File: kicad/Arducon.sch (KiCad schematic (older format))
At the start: 67 parts, among them J101 To Radio, J102 DB9 Female, J103 To Antenna, J104 Conn_01x08, J105 Conn_01x08, J106 Logic Level, J107 External Power Source, J108 Controlled Power, J109 Conn_01x01, J110 Conn_01x01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

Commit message: BOM Updates
Updated BOM
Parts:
- SJ110: renamed from SJ101; Link (none) -> np; Part No. (none) -> np
- SJ111: renamed from SJ102; Link (none) -> np; Part No. (none) -> np
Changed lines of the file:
@@
 Sheet 1 2
 Title "Arducon"
-Date "2021-02-24"
+Date "2021-03-03"
 Rev "P2.0"
 Comp ""
@@
 EXTERNAL_PWR_SOURCE
 $Comp
-L Jumper:SolderJumper_3_Bridged12 SJ102
+L Jumper:SolderJumper_3_Bridged12 SJ111
 U 1 1 60436DAC
 P 2150 6800
-F 0 "SJ102" V 2150 6867 50  0000 L CNN
+F 0 "SJ111" V 2150 6867 50  0000 L CNN
 F 1 "SolderJumper_3_Bridged12" V 2195 6868 50  0001 L CNN
 F 2 "Wire_Connections_Bridges:Solder-Jumperx3-NC_1-2_SMD-Pad_Small" H 2150 6800 50  0001 C CNN
-F 3 "~" H 2150 6800 50  0001 C CNN
+F 3 "" H 2150 6800 50  0001 C CNN
+F 4 "np" H 2150 6800 50  0001 C CNN "Part No."
+F 5 "np" H 2150 6800 50  0001 C CNN "Link"
 	1    2150 6800
 	0    -1   1    0
@@
 	3700 4750 3700 6150
 $Comp
-L Jumper:SolderJumper_3_Bridged12 SJ101
+L Jumper:SolderJumper_3_Bridged12 SJ110
 U 1 1 6050CA09
 P 2300 5550
-F 0 "SJ101" H 2300 5663 50  0000 C CNN
+F 0 "SJ110" H 2300 5663 50  0000 C CNN
 F 1 "SolderJumper_3_Bridged12" V 2345 5618 50  0001 L CNN
 F 2 "Wire_Connections_Bridges:Solder-Jumperx3-NC_1-2_SMD-Pad_Small" H 2300 5550 50  0001 C CNN
-F 3 "~" H 2300 5550 50  0001 C CNN
+F 3 "" H 2300 5550 50  0001 C CNN
+F 4 "np" H 2300 5550 50  0001 C CNN "Part No."
+F 5 "np" H 2300 5550 50  0001 C CNN "Link"
 	1    2300 5550
 	-1   0    0    1

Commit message: PCB Updates
PCB, Schematic, and BOM Updates
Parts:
- removed SJ109: SolderJumper_2_Open, Wire_Connections_Bridges:Solder-Jumper-NO-SMD-Pad_Small, symbol Jumper:SolderJumper_2_Open
- added SW102: 5V/12V, Buttons_Switches_SMD:SW_SPDT_PCM12, symbol Switch:SW_SPDT
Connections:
- net Controlled_Power: no longer J102.2
- net EXT_BATTERY: now also SW102.3 (C); no longer J102.7
- net Vproc: now also SW102.1 (A); no longer J102.4
- net DTR: now reaches MOD101.30 (DTR)
- net DTR: now also J102.2
- net CW_KEY: now reaches J106.3 (Pin_3), SJ110.2 (C)
- net CW_KEY: now also J102.4
- net ~RTC_INT~ renamed PD3
- new net RADIO_V+: J102.7, SW102.2 (B)
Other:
- moved on the sheet: C103, Q101, R101, R102, R104, RV101, SJ102

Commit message: Gerbers
Small updates to silkscreen layer
Small updates to schematic
Generated Gerber files for JLCPCB
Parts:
- removed SJ111: SolderJumper_3_Bridged12, Wire_Connections_Bridges:Solder-Jumperx3-NC_1-2_SMD-Pad_Small, symbol Jumper:SolderJumper_3_Bridged12
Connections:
- net RADIO_V+ is gone; now on net Power_In: J102.7, SW102.2 (B)
- net Power_In: now reaches R107.2
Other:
- moved on the sheet: C103, C109, R101, R102, R107, R108, RV101, SJ102, SW102

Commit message: TVS Diode Substitution
Substituted an 0603 footprint TVS diode for the smaller TVS diodes that were prone to tombstoning.
Updated BOM
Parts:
- D103, D104, D105, D106, D107: value ESD9B5.0ST5G -> CG0603MLC-05LECT-ND; Link <a href=\"https://www.digikey.com/products/en?keywords=ESD9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 -> <a href=\"https://www.digikey.com/products/en?keywords=CG06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; Part No. ESD9B5.0ST5GOSCT-ND -> CG0603MLC-05LECT-ND
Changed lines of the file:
@@
 P 2150 8200
 F 0 "D103" H 2150 8121 50  0000 R CNN
-F 1 "ESD9B5.0ST5G" V 2105 8121 50  0001 R CNN
+F 1 "CG0603MLC-05LECT-ND" V 2105 8121 50  0001 R CNN
 F 2 "Resistors_SMD:R_0603" H 2150 8200 50  0001 C CNN
-F 3 "https://www.onsemi.com/pub/Collateral/ESD9B-D.PDF" H 2150 8200 50  0001 C CNN
-F 4 "ESD9B5.0ST5GOSCT-ND" H 2150 8200 50  0001 C CNN "Part No."
-F 5 "<a href=\"https://www.digikey.com/products/en?keywords=ESD9B5.0ST5GOSCT-ND\">Link</a>" H 2150 8200 50  0001 C CNN "Link"
+F 3 "" H 2150 8200 50  0001 C CNN
+F 4 "CG0603MLC-05LECT-ND" H 2150 8200 50  0001 C CNN "Part No."
+F 5 "<a href=\"https://www.digikey.com/products/en?keywords=CG0603MLC-05LECT-ND\">Link</a>" H 2150 8200 50  0001 C CNN "Link"
 	1    2150 8200
 	0    -1   -1   0
@@
 P 2400 8200
 F 0 "D104" H 2400 8121 50  0000 R CNN
-F 1 "ESD9B5.0ST5G" V 2355 8121 50  0001 R CNN
+F 1 "CG0603MLC-05LECT-ND" V 2355 8121 50  0001 R CNN
 F 2 "Resistors_SMD:R_0603" H 2400 8200 50  0001 C CNN
-F 3 "https://www.onsemi.com/pub/Collateral/ESD9B-D.PDF" H 2400 8200 50  0001 C CNN
-F 4 "ESD9B5.0ST5GOSCT-ND" H 2400 8200 50  0001 C CNN "Part No."
-F 5 "<a href=\"https://www.digikey.com/products/en?keywords=ESD9B5.0ST5GOSCT-ND\">Link</a>" H 2400 8200 50  0001 C CNN "Link"
+F 3 "" H 2400 8200 50  0001 C CNN
+F 4 "CG0603MLC-05LECT-ND" H 2400 8200 50  0001 C CNN "Part No."
+F 5 "<a href=\"https://www.digikey.com/products/en?keywords=CG0603MLC-05LECT-ND\">Link</a>" H 2400 8200 50  0001 C CNN "Link"
 	1    2400 8200
 	0    -1   -1   0
@@
 P 2650 8200
 F 0 "D105" H 2650 8121 50  0000 R CNN
-F 1 "ESD9B5.0ST5G" V 2605 8121 50  0001 R CNN
+F 1 "CG0603MLC-05LECT-ND" V 2605 8121 50  0001 R CNN
 F 2 "Resistors_SMD:R_0603" H 2650 8200 50  0001 C CNN
-F 3 "https://www.onsemi.com/pub/Collateral/ESD9B-D.PDF" H 2650 8200 50  0001 C CNN
-F 4 "ESD9B5.0ST5GOSCT-ND" H 2650 8200 50  0001 C CNN "Part No."
-F 5 "<a href=\"https://www.digikey.com/products/en?keywords=ESD9B5.0ST5GOSCT-ND\">Link</a>" H 2650 8200 50  0001 C CNN "Link"
+F 3 "" H 2650 8200 50  0001 C CNN
+F 4 "CG0603MLC-05LECT-ND" H 2650 8200 50  0001 C CNN "Part No."
+F 5 "<a href=\"https://www.digikey.com/products/en?keywords=CG0603MLC-05LECT-ND\">Link</a>" H 2650 8200 50  0001 C CNN "Link"
 	1    2650 8200
 	0    -1   -1   0
@@
 P 2900 8200
 F 0 "D106" H 2900 8121 50  0000 R CNN
-F 1 "ESD9B5.0ST5G" V 2855 8121 50  0001 R CNN
+F 1 "CG0603MLC-05LECT-ND" V 2855 8121 50  0001 R CNN
 F 2 "Resistors_SMD:R_0603" H 2900 8200 50  0001 C CNN
-F 3 "https://www.onsemi.com/pub/Collateral/ESD9B-D.PDF" H 2900 8200 50  0001 C CNN
-F 4 "ESD9B5.0ST5GOSCT-ND" H 2900 8200 50  0001 C CNN "Part No."
-F 5 "<a href=\"https://www.digikey.com/products/en?keywords=ESD9B5.0ST5GOSCT-ND\">Link</a>" H 2900 8200 50  0001 C CNN "Link"
+F 3 "" H 2900 8200 50  0001 C CNN
+F 4 "CG0603MLC-05LECT-ND" H 2900 8200 50  0001 C CNN "Part No."
+F 5 "<a href=\"https://www.digikey.com/products/en?keywords=CG0603MLC-05LECT-ND\">Link</a>" H 2900 8200 50  0001 C CNN "Link"
 	1    2900 8200
 	0    -1   -1   0
@@
 P 3150 8200
 F 0 "D107" H 3150 8121 50  0000 R CNN
-F 1 "ESD9B5.0ST5G" V 3105 8121 50  0001 R CNN
+F 1 "CG0603MLC-05LECT-ND" V 3105 8121 50  0001 R CNN
 F 2 "Resistors_SMD:R_0603" H 3150 8200 50  0001 C CNN
-F 3 "https://www.onsemi.com/pub/Collateral/ESD9B-D.PDF" H 3150 8200 50  0001 C CNN
-F 4 "ESD9B5.0ST5GOSCT-ND" H 3150 8200 50  0001 C CNN "Part No."
-F 5 "<a href=\"https://www.digikey.com/products/en?keywords=ESD9B5.0ST5GOSCT-ND\">Link</a>" H 3150 8200 50  0001 C CNN "Link"
+F 3 "" H 3150 8200 50  0001 C CNN
+F 4 "CG0603MLC-05LECT-ND" H 3150 8200 50  0001 C CNN "Part No."
+F 5 "<a href=\"https://www.digikey.com/products/en?keywords=CG0603MLC-05LECT-ND\">Link</a>" H 3150 8200 50  0001 C CNN "Link"
 	1    3150 8200
 	0    -1   -1   0

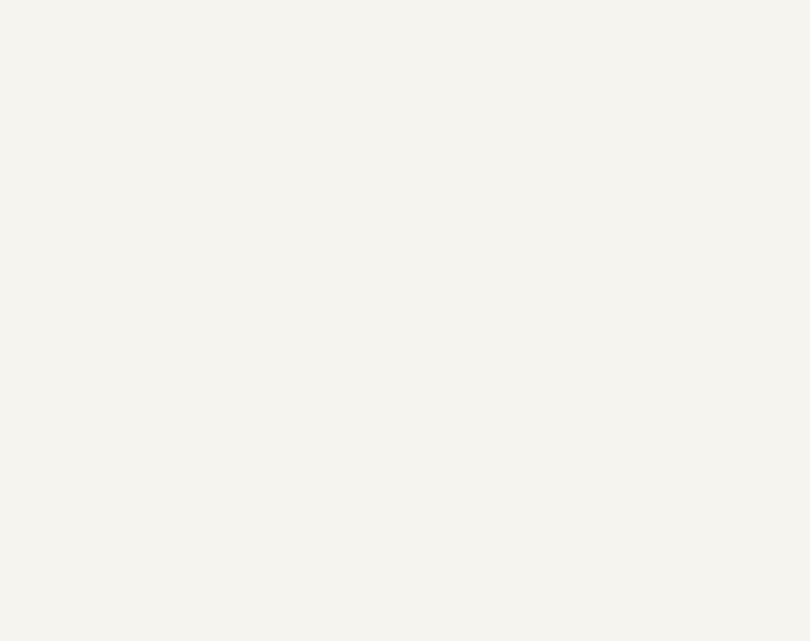
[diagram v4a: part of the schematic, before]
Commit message: Added FTDI Adapter
Added a small FTDI Adapter board that will allow standard FTDI programming cables to plug into the D-connector
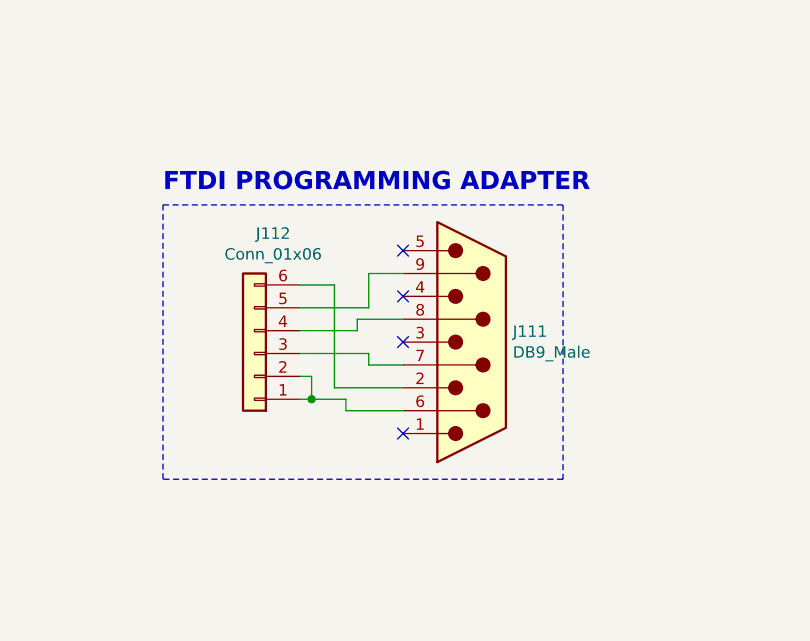
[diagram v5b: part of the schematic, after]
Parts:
- added J111: DB9_Male, Connect:DB9F_CI, symbol Connector:DB9_Male
- added J112: Conn_01x06, Pin_Headers:Pin_Header_Angled_1x06, symbol Connector_Generic:Conn_01x06
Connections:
- new net: J111.6, J112.1 (Pin_1), J112.2 (Pin_2)
- new net: J111.7, J112.3 (Pin_3)
- new net: J111.8, J112.4 (Pin_4)
- new net: J111.9, J112.5 (Pin_5)
- new net: J111.2, J112.6 (Pin_6)
- no-connect marks 14 -> 18
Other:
- note added: "FTDI PROGRAMMING ADAPTER"
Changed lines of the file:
@@
 Text GLabel 2650 6250 0    39   Input ~ 0
 Power_In
+$Comp
+L Connector_Generic:Conn_01x06 J112
+U 1 1 604658B7
+P 8200 8450
+F 0 "J112" H 8118 7925 50  0000 C CNN
+F 1 "Conn_01x06" H 8118 8016 50  0000 C CNN
+F 2 "Pin_Headers:Pin_Header_Angled_1x06" H 8200 8450 50  0001 C CNN
+F 3 "" H 8200 8450 50  0001 C CNN
+F 4 "929550-01-06-ND" H 8200 8450 50  0001 C CNN "Part No."
+F 5 "<a href=\"https://www.digikey.com/products/en?keywords=929550-01-06-ND\">Link</a>" H 8200 8450 50  0001 C CNN "Link"
+	1    8200 8450
+	-1   0    0    1
+$EndComp
+$Comp
+L Connector:DB9_Male J111
+U 1 1 60486C18
+P 9150 8400
+F 0 "J111" H 9330 8446 50  0000 L CNN
+F 1 "DB9_Male" H 9330 8355 50  0000 L CNN
+F 2 "Connect:DB9F_CI" H 9150 8400 50  0001 C CNN
+F 3 "" H 9150 8400 50  0001 C CNN
+F 4 "609-5908-ND" H 9150 8400 50  0001 C CNN "Part No."
+F 5 "<a href=\"https://www.digikey.com/products/en?keywords=609-5908-ND\">Link</a>" H 9150 8400 50  0001 C CNN "Link"
+	1    9150 8400
+	1    0    0    -1
+$EndComp
+Wire Wire Line
+	8400 8650 8450 8650
+Wire Wire Line
+	8600 8650 8600 8700
+Wire Wire Line
+	8600 8700 8850 8700
+Wire Wire Line
+	8400 8450 8700 8450
+Wire Wire Line
+	8700 8450 8700 8500
+Wire Wire Line
+	8700 8500 8850 8500
+Wire Wire Line
+	8400 8350 8650 8350
+Wire Wire Line
+	8400 8250 8700 8250
+Wire Wire Line
+	8400 8150 8550 8150
+Wire Wire Line
+	8550 8150 8550 8600
+Wire Wire Line
+	8550 8600 8850 8600
+Wire Wire Line
+	8400 8550 8450 8550
+Wire Wire Line
+	8450 8550 8450 8650
+Connection ~ 8450 8650
+Wire Wire Line
+	8450 8650 8600 8650
+NoConn ~ 8850 8000
+NoConn ~ 8850 8200
+NoConn ~ 8850 8400
+NoConn ~ 8850 8800
+Text Notes 7800 7750 0    79   ~ 16
+FTDI PROGRAMMING ADAPTER
+Wire Notes Line
+	7800 7800 9550 7800
+Wire Notes Line
+	9550 7800 9550 9000
+Wire Notes Line
+	9550 9000 7800 9000
+Wire Notes Line
+	7800 9000 7800 7800
+Wire Wire Line
+	8650 8350 8650 8300
+Wire Wire Line
+	8650 8300 8850 8300
+Wire Wire Line
+	8700 8250 8700 8100
+Wire Wire Line
+	8700 8100 8850 8100
 Wire Bus Line
 	6300 4600 6300 7300

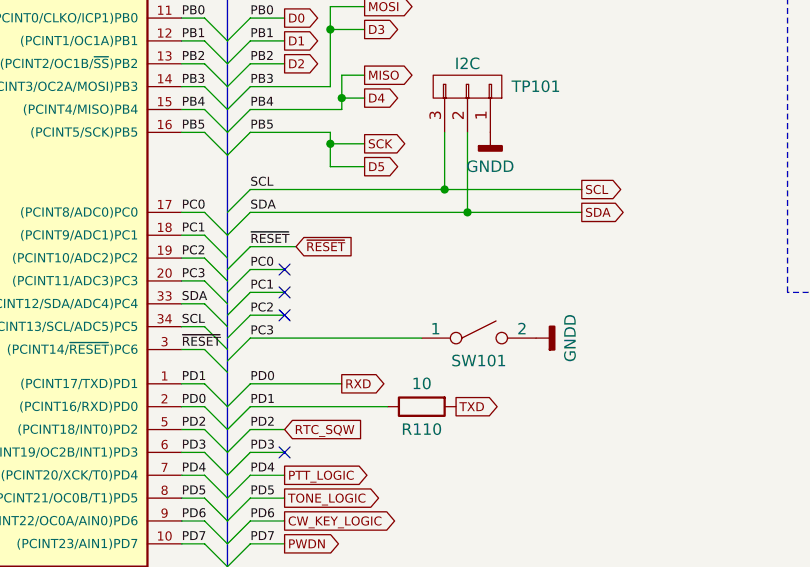
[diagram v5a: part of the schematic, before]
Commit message: Added LED
Added an LED to the schematic and PCB
Updated BOM
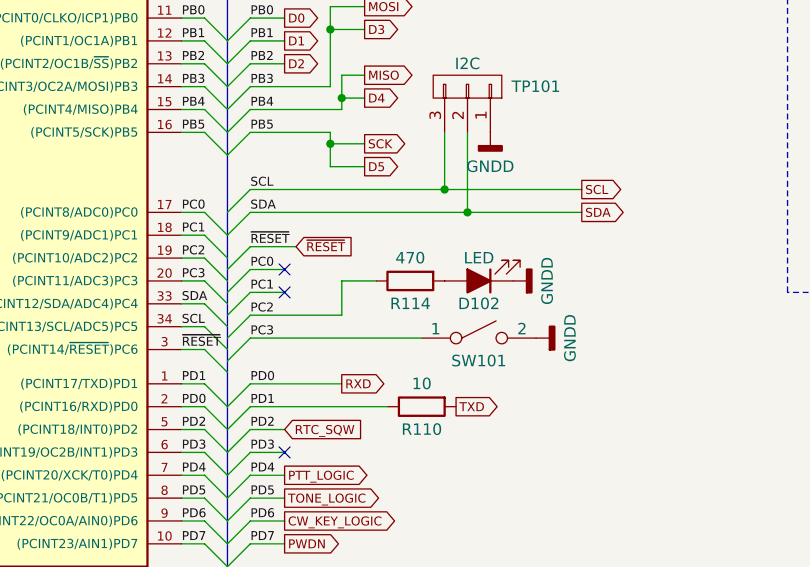
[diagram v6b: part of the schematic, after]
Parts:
- added D102: LED, LEDs:LED_0805, symbol Device:LED_ALT
- added R114: 470, Resistors_SMD:R_0805, symbol Device:R
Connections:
- net GND: now also D102.1 (K)
- net PC2: now also R114.1
- new net: D102.2 (A), R114.2
- no-connect marks 18 -> 17
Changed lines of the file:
@@
 	6550 6000 6400 6000
-Wire Wire Line
-	6550 6100 6400 6100
 Wire Wire Line
 	6550 5000 6400 5000
@@
 NoConn ~ 6550 5900
 NoConn ~ 6550 6000
-NoConn ~ 6550 6100
 Wire Wire Line
 	6400 6200 7150 6200
@@
 Wire Wire Line
 	8700 8100 8850 8100
+$Comp
+L Device:LED_ALT D102
+U 1 1 604C2CC2
+P 7400 5950
+F 0 "D102" H 7400 6050 50  0000 C CNN
+F 1 "LED" H 7400 5850 50  0000 C CNN
+F 2 "LEDs:LED_0805" H 7400 5950 50  0001 C CNN
+F 3 "" H 7400 5950 50  0001 C CNN
+F 4 "732-4984-1-ND" H 7400 5950 50  0001 C CNN "Part No."
+F 5 "<a href=\"https://www.digikey.com/products/en?keywords=732-4984-1-ND\">Link</a>" H 7400 5950 50  0001 C CNN "Link"
+	1    7400 5950
+	-1   0    0    1
+$EndComp
+$Comp
+L power:GNDD #PWR0158
+U 1 1 604C760D
+P 7550 5950
+F 0 "#PWR0158" H 7550 5700 50  0001 C CNN
+F 1 "GNDD" H 7550 5800 50  0000 C CNN
+F 2 "" H 7550 5950 50  0000 C CNN
+F 3 "" H 7550 5950 50  0000 C CNN
+	1    7550 5950
+	0    -1   -1   0
+$EndComp
+Wire Wire Line
+	6800 6100 6800 5950
+Wire Wire Line
+	6400 6100 6800 6100
+$Comp
+L Device:R R114
+U 1 1 605220BB
+P 7100 5950
+F 0 "R114" V 7200 5950 50  0000 C CNN
+F 1 "470" V 7000 5950 50  0000 C CNN
+F 2 "Resistors_SMD:R_0805" H 7030 5950 50  0001 C CNN
+F 3 "" H 7100 5950 50  0001 C CNN
+F 4 "311-470CRCT-ND" H 7100 5950 60  0001 C CNN "Part No."
+F 5 "<a href=\"https://www.digikey.com/products/en?keywords=311-470CRCT-ND\">Link</a>" H 7100 5950 60  0001 C CNN "Link"
+	1    7100 5950
+	0    -1   1    0
+$EndComp
+Wire Wire Line
+	6800 5950 6950 5950
 Wire Bus Line
 	6300 4600 6300 7300

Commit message: Cleanup KiCad
o Cleanup of KiCad schematic
o Added BOM scripts to GitHub
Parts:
- BT101: symbol Arducon-rescue:Battery_Single_Cell -> Device:Battery_Single_Cell
- MOD101: symbol Arducon-rescue:Arduino_Pro_Mini-MCU_Module -> MCU_Module:Arduino_Pro_Mini-MCU_Module; Description (none) -> Arduino Pro Mini 328 - 5V/16 MHz; Manufacturer (none) -> AdaFruit Industries; Manufacturer PN (none) -> 2378
- P101: symbol Arducon-rescue:CONN_02X03 -> Connector_Generic:Conn_02x03_Odd_Even
- Q102: symbol Arducon-rescue:LMN200B01-Two-band-Tx -> Power_Protection:LMN200B01
- RV101: symbol Arducon-rescue:POT -> Device:R_POT
- SW101: symbol Arducon-rescue:SPST_small -> Switch:SPST_small
- TP101: symbol Arducon-rescue:CONN_01X03 -> Connector_Generic:Conn_01x03
- U102: symbol Arducon-rescue:CD74HC4050M96-74xx -> Logic_LevelTranslator:CD74HC4050M96-74xx
- U103: symbol Arducon-rescue:RV-3028-C7-special -> Timer_RTC:RV-3028-C7
- U104: symbol Arducon-rescue:F1975-RF -> RF:F1975NCGI
- W101, W102: symbol Arducon-rescue:CONN_01X01 -> Connector_Generic:Conn_01x01
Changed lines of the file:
@@
 ~RESET~
 $Comp
-L Arducon-rescue:CONN_02X03 P101
+L Connector_Generic:Conn_02x03_Odd_Even P101
 U 1 1 57AD5B1A
-P 5250 7800
-F 0 "P101" H 5250 8000 50  0000 C CNN
-F 1 "ISP/PDI" H 5250 7600 50  0000 C CNN
-F 2 "Pin_Headers:SM_Pin_Header_Straight_2x03" H 5250 6600 50  0001 C CNN
-F 3 "http://katalog.we-online.de/em/datasheet/6100xx21121.pdf" H 5250 6600 50  0001 C CNN
-F 4 "609-3487-1-ND" H 5250 7800 60  0001 C CNN "Part No."
-F 5 "<a href=\"https://www.digikey.com/products/en?keywords=609-3487-1-ND\">Link</a>" H 5250 7800 60  0001 C CNN "Link"
-	1    5250 7800
+P 5300 7800
+F 0 "P101" H 5300 8000 50  0000 C CNN
+F 1 "ISP/PDI" H 5300 7600 50  0000 C CNN
+F 2 "Pin_Headers:SM_Pin_Header_Straight_2x03" H 5300 6600 50  0001 C CNN
+F 3 "http://katalog.we-online.de/em/datasheet/6100xx21121.pdf" H 5300 6600 50  0001 C CNN
+F 4 "609-3487-1-ND" H 5300 7800 60  0001 C CNN "Part No."
+F 5 "<a href=\"https://www.digikey.com/products/en?keywords=609-3487-1-ND\">Link</a>" H 5300 7800 60  0001 C CNN "Link"
+	1    5300 7800
 	-1   0    0    1
 $EndComp
@@
 $EndComp
 $Comp
-L Arducon-rescue:Vproc #PWR0127
+L power:Vproc #PWR0127
 U 1 1 591CAC09
 P 3950 4300
@@
 $EndComp
 $Comp
-L Arducon-rescue:CONN_01X01 W101
+L Connector_Generic:Conn_01x01 W101
 U 1 1 59FF6C44
 P 11800 9850
@@
 $EndComp
 $Comp
-L Arducon-rescue:CONN_01X01 W102
+L Connector_Generic:Conn_01x01 W102
 U 1 1 59FF6D51
 P 11800 10050
@@
 $EndComp
 $Comp
-L Arducon-rescue:CONN_01X03 TP101
+L Connector_Generic:Conn_01x03 TP101
 U 1 1 5A0894A0
 P 7350 5100
@@
 $EndComp
 $Comp
-L Arducon-rescue:Vproc #PWR0107
+L power:Vproc #PWR0107
 U 1 1 5AB7DABB
 P 7350 2300
@@
 $EndComp
 $Comp
-L Arducon-rescue:Battery_Single_Cell BT101
+L Device:Battery_Single_Cell BT101
 U 1 1 5BCD438E
 P 5500 2700
@@
 $EndComp
 $Comp
-L Arducon-rescue:Vproc #PWR0144
+L power:Vproc #PWR0144
 U 1 1 5C60DF91
 P 5600 7650
@@
 SDA
 $Comp
-L Arducon-rescue:RV-3028-C7-special U103
+L Timer_RTC:RV-3028-C7 U103
 U 1 1 5F9A0888
 P 7350 3450
@@
 TONE_LOGIC
 $Comp
-L Arducon-rescue:POT RV101
+L Device:R_POT RV101
 U 1 1 5F9CC9A1
 P 4300 2250
-F 0 "RV101" H 4300 2170 50  0000 C CNN
-F 1 "10k" H 4300 2250 50  0000 C CNN
+F 0 "RV101" H 4100 2150 50  0000 C CNN
+F 1 "10k" H 4150 2250 50  0000 C CNN
 F 2 "Potentiometers:Potentiometer_ST32ET_Handsolder" H 4300 2250 50  0001 C CNN
 F 3 "" H 4300 2250 50  0000 C CNN
@@
 F 5 "<a href=\"https://www.digikey.com/products/en?keywords=TC33X-103ECT-ND\">Link</a>" H 4300 2250 50  0001 C CNN "Link"
 	1    4300 2250
-	0    -1   -1   0
+	-1   0    0    1
 $EndComp
 $Comp
@@
 $EndComp
 $Comp
-L Arducon-rescue:SPST_small SW101
+L Switch:SPST_small SW101
 U 1 1 5F9DCC49
 P 7400 6200
@@
 $EndComp
 $Comp
-L Arducon-rescue:Arduino_Pro_Mini-MCU_Module MOD101
+L MCU_Module:Arduino_Pro_Mini-MCU_Module MOD101
 U 1 1 5FC82DF4
 P 5100 5900
@@
 F 4 "1568-1055-ND" H 5100 5900 50  0001 C CNN "Part No."
 F 5 "<a href=\"https://www.digikey.com/products/en?keywords=1568-1055-ND\">Link</a>" H 5100 5900 50  0001 C CNN "Link"
+F 6 "AdaFruit Industries" H 5100 5900 50  0001 C CNN "Manufacturer"
+F 7 "2378" H 5100 5900 50  0001 C CNN "Manufacturer PN"
+F 8 "Arduino Pro Mini 328 - 5V/16 MHz" H 5100 5900 50  0001 C CNN "Description"
 	1    5100 5900
 	1    0    0    -1
@@
 $EndComp
 $Comp
-L Arducon-rescue:Vproc #PWR0134
+L power:Vproc #PWR0134
 U 1 1 5FF2E22F
 P 3100 4400
@@
 	3850 7100 3900 7100
 $Comp
-L Arducon-rescue:F1975-RF U104
+L RF:F1975NCGI U104
 U 1 1 5FF7DEC4
 P 14100 2800
@@
 $EndComp
 $Comp
-L Arducon-rescue:CD74HC4050M96-74xx U102
+L Logic_LevelTranslator:CD74HC4050M96-74xx U102
 U 1 1 5FFA3B6A
 P 10350 5250
@@
 $EndComp
 $Comp
-L Arducon-rescue:CD74HC4050M96-74xx U102
+L Logic_LevelTranslator:CD74HC4050M96-74xx U102
 U 2 1 5FFA7F9B
 P 10350 4700
@@
 $EndComp
 $Comp
-L Arducon-rescue:CD74HC4050M96-74xx U102
+L Logic_LevelTranslator:CD74HC4050M96-74xx U102
 U 3 1 5FFA8DF3
 P 10350 4150
@@
 $EndComp
 $Comp
-L Arducon-rescue:CD74HC4050M96-74xx U102
+L Logic_LevelTranslator:CD74HC4050M96-74xx U102
 U 4 1 5FFA9DCC
 P 10350 3700
@@
 $EndComp
 $Comp
-L Arducon-rescue:CD74HC4050M96-74xx U102
+L Logic_LevelTranslator:CD74HC4050M96-74xx U102
 U 5 1 5FFAB336
 P 10350 3200
@@
 $EndComp
 $Comp
-L Arducon-rescue:CD74HC4050M96-74xx U102
+L Logic_LevelTranslator:CD74HC4050M96-74xx U102
 U 6 1 5FFAC3C8
 P 10350 2700
@@
 	4000 3200 4000 3100
 $Comp
-L Arducon-rescue:LMN200B01-Two-band-Tx Q102
+L Power_Protection:LMN200B01 Q102
 U 1 1 5FC59E4B
 P 13550 7600
@@
 $EndComp
 $Comp
-L Arducon-rescue:Vproc #PWR0113
+L power:Vproc #PWR0113
 U 1 1 5FFE7858
 P 9750 1450
@@
 NoConn ~ 4200 5600
 $Comp
-L Arducon-rescue:Vproc #PWR0156
+L power:Vproc #PWR0156
 U 1 1 5FDC95A5
 P 2900 2550
@@
 F 4 "MMBT2222ATPMSCT-ND" H 4100 3400 50  0001 C CNN "Part No."
 F 5 "<a href=\"https://www.digikey.com/products/en?keywords=MMBT2222ATPMSCT-ND\">Link</a>" H 4100 3400 50  0001 C CNN "Link"
+F 6 "" H 4100 3400 50  0001 C CNN "Manufacturer"
+F 7 "" H 4100 3400 50  0001 C CNN "Manufacturer PN"
+F 8 "" H 4100 3400 50  0001 C CNN "Description"
 	1    4100 3400
 	-1   0    0    -1
@@
 F 4 "MMBT2222ATPMSCT-ND" H 2050 5900 50  0001 C CNN "Part No."
 F 5 "<a href=\"https://www.digikey.com/products/en?keywords=MMBT2222ATPMSCT-ND\">Link</a>" H 2050 5900 50  0001 C CNN "Link"
+F 6 "" H 2050 5900 50  0001 C CNN "Manufacturer"
 	1    2050 5900
 	-1   0    0    -1
@@
 $EndComp
 $Comp
-L Arducon-rescue:Vproc #PWR0146
+L power:Vproc #PWR0146
 U 1 1 605016E9
 P 6350 2950
